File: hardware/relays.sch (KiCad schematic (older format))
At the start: 203 parts

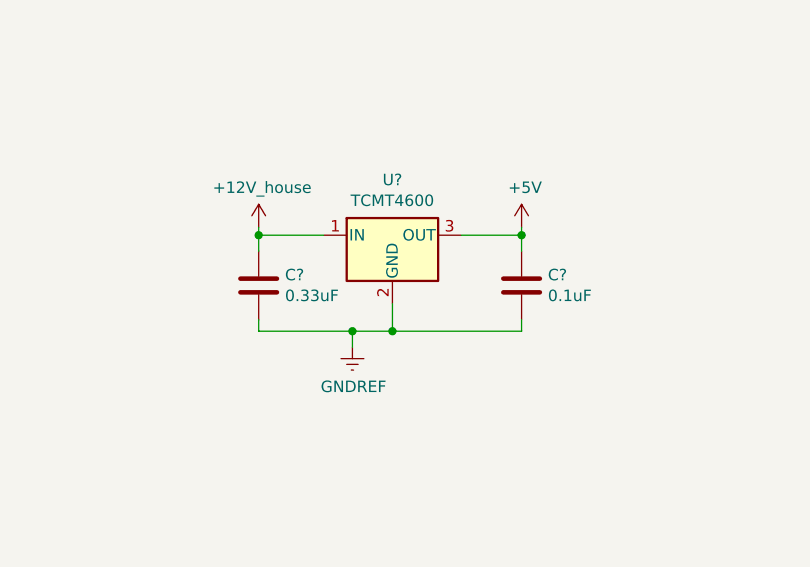
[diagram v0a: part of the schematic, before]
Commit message: hardware: add 5V domain for house and truck supplies
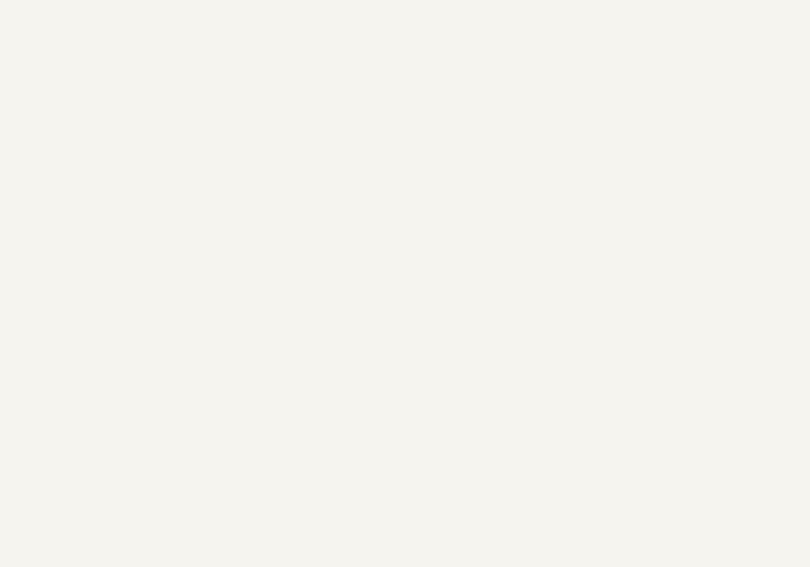
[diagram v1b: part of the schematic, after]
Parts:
- removed C?: 0.33uF, Capacitor_SMD:C_0805_2012Metric_Pad1.18x1.45mm_HandSolder, symbol Device:C
- removed C?: 0.1uF, Capacitor_SMD:C_0805_2012Metric_Pad1.18x1.45mm_HandSolder, symbol Device:C
- removed U?: TCMT4600, Package_SO:SOP-16_4.55x10.3mm_P1.27mm, symbol Regulator_Linear:L7805
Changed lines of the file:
@@
-$EndComp
-$Comp
-L Regulator_Linear:L7805 U?
-U 1 1 6096161B
-P 29230 5335
-F 0 "U?" H 29230 5577 50  0000 C CNN
-F 1 "TCMT4600" H 29230 5486 50  0000 C CNN
-F 2 "Package_SO:SOP-16_4.55x10.3mm_P1.27mm" H 29255 5185 50  0001 L CIN
-F 3 "http://www.vishay.com/docs/83512/tcmt1600.pdf" H 29230 5285 50  0001 C CNN
-	1    29230 5335
-	1    0    0    -1
-$EndComp
-$Comp
-L Device:C C?
-U 1 1 60963BB6
-P 28645 5555
-F 0 "C?" H 28760 5601 50  0000 L CNN
-F 1 "0.33uF" H 28760 5510 50  0000 L CNN
-F 2 "Capacitor_SMD:C_0805_2012Metric_Pad1.18x1.45mm_HandSolder" H 28683 5405 50  0001 C CNN
-F 3 "~" H 28645 5555 50  0001 C CNN
-	1    28645 5555
-	1    0    0    -1
-$EndComp
-$Comp
-L Device:C C?
-U 1 1 60964243
-P 29795 5555
-F 0 "C?" H 29910 5601 50  0000 L CNN
-F 1 "0.1uF" H 29910 5510 50  0000 L CNN
-F 2 "Capacitor_SMD:C_0805_2012Metric_Pad1.18x1.45mm_HandSolder" H 29833 5405 50  0001 C CNN
-F 3 "~" H 29795 5555 50  0001 C CNN
-	1    29795 5555
-	1    0    0    -1
-$EndComp
-Wire Wire Line
-	29530 5335 29795 5335
-Wire Wire Line
-	28645 5335 28930 5335
-Wire Wire Line
-	28645 5705 28645 5755
-Wire Wire Line
-	28645 5755 29055 5755
-Wire Wire Line
-	29795 5755 29795 5705
-Connection ~ 29230 5755
-Wire Wire Line
-	29230 5755 29795 5755
-$Comp
-L power:GNDREF #PWR?
-U 1 1 609665C9
-P 29055 5825
-F 0 "#PWR?" H 29055 5575 50  0001 C CNN
-F 1 "GNDREF" H 29060 5652 50  0000 C CNN
-F 2 "" H 29055 5825 50  0001 C CNN
-F 3 "" H 29055 5825 50  0001 C CNN
-	1    29055 5825
-	1    0    0    -1
-$EndComp
-Wire Wire Line
-	29055 5825 29055 5755
-Connection ~ 29055 5755
-Wire Wire Line
-	29055 5755 29230 5755
-Wire Wire Line
-	29230 5635 29230 5755
-Wire Wire Line
-	28645 5335 28645 5405
-Wire Wire Line
-	29795 5335 29795 5405
-Wire Wire Line
-	29795 5335 29795 5300
-Connection ~ 29795 5335
-Wire Wire Line
-	28645 5335 28645 5300
-Connection ~ 28645 5335
-$Comp
-L switchboard:+12V_house #PWR?
-U 1 1 6096CA71
-P 28645 5300
-F 0 "#PWR?" H 28645 5150 50  0001 C CNN
-F 1 "+12V_house" H 28660 5473 50  0000 C CNN
-F 2 "" H 28645 5300 50  0001 C CNN
-F 3 "" H 28645 5300 50  0001 C CNN
-	1    28645 5300
-	1    0    0    -1
-$EndComp
-$Comp
-L power:+5V #PWR?
-U 1 1 6096DC54
-P 29795 5300
-F 0 "#PWR?" H 29795 5150 50  0001 C CNN
-F 1 "+5V" H 29810 5473 50  0000 C CNN
-F 2 "" H 29795 5300 50  0001 C CNN
-F 3 "" H 29795 5300 50  0001 C CNN
-	1    29795 5300
-	1    0    0    -1
 $EndComp
 $Comp

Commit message: hardware: use 5V_house/truck nets for load drivers
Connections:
- net +5V: no longer U?.16

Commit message: hardware: fix weird bug with VN750 symbol
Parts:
- removed U? (x50): TCMT4600, Package_SO:SOP-16_4.55x10.3mm_P1.27mm, symbol switchboard:VN750
- added U? (x50): VN750, switchboard:VN750-B513TR, symbol switchboard:VN750
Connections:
- net AUX_1_OUT0: now also U?.3
- net AUX_1_OUT1: now also U?.5
- net AUX_2_OUT0: now also U?.3
- net AUX_2_OUT1: now also U?.5
- net AUX_3_OUT0: now also U?.3
- net AUX_3_OUT1: now also U?.5
- net AUX_4_OUT0: now also U?.3
- net AUX_4_OUT1: now also U?.5
- net BACKUP_ALARM0: now also U?.3
- net BACKUP_ALARM1: now also U?.5
- net BAR_LIGHT0: now also U?.3
- net BAR_LIGHT1: now also U?.5
- net BENCH_DOME_A0: now also U?.3
- net BENCH_DOME_A1: now also U?.5
- net BENCH_DOME_B0: now also U?.3
- net BENCH_DOME_B1: now also U?.5
- net COMP_1_LIGHT0: now also U?.3
- net COMP_1_LIGHT1: now also U?.5
- net COMP_2_LIGHT0: now also U?.3
- net COMP_2_LIGHT1: now also U?.5
- net COMP_3_LIGHT0: now also U?.3
- net COMP_3_LIGHT1: now also U?.5
- net COMP_4_LIGHT0: now also U?.3
- net COMP_4_LIGHT1: now also U?.5
- net COMP_5_LIGHT0: now also U?.3
- net COMP_5_LIGHT1: now also U?.5
- net COT_DOME_A0: now also U?.3
- net COT_DOME_A1: now also U?.5
- net COT_DOME_B0: now also U?.3
- net COT_DOME_B1: now also U?.5
- net CURB_FRONT_RED0: now also U?.3
- net CURB_FRONT_RED1: now also U?.5
- net CURB_REAR_RED0: now also U?.3
- net CURB_REAR_RED1: now also U?.5
- net DRIVER_FLOOD_A0: now also U?.3
- net DRIVER_FLOOD_A1: now also U?.5
- net DRIVER_FLOOD_B0: now also U?.3
- net DRIVER_FLOOD_B1: now also U?.5
- net FOG_CURB0: now also U?.3
- net FOG_CURB1: now also U?.5
- net FOG_STREET0: now also U?.3
- net FOG_STREET1: now also U?.5
- net GNDREF: now also U?.1 (GND), U?.1 (GND), U?.1 (GND), U?.1 (GND), U?.1 (GND), U?.1 (GND), U?.1 (GND), U?.1 (GND), U?.1 (GND), U?.1 (GND), U?.1 (GND), U?.1 (GND), U?.1 (GND), U?.1 (GND), U?.1 (GND), U?.1 (GND), U?.1 (GND), U?.1 (GND), U?.1 (GND), U?.1 (GND), U?.1 (GND), U?.1 (GND), U?.1 (GND), U?.1 (GND), U?.1 (GND), U?.1 (GND), U?.1 (GND), U?.1 (GND), U?.1 (GND), U?.1 (GND), U?.1 (GND), U?.1 (GND), U?.1 (GND), U?.1 (GND), U?.1 (GND), U?.1 (GND), U?.1 (GND), U?.1 (GND), U?.1 (GND), U?.1 (GND), U?.1 (GND), U?.1 (GND), U?.1 (GND), U?.1 (GND), U?.1 (GND), U?.1 (GND), U?.1 (GND), U?.1 (GND), U?.1 (GND), U?.1 (GND)
- net GRILLE_STROBE0: now also U?.3
- net GRILLE_STROBE1: now also U?.5
- net HEADLAMP_HI_L0: now also U?.3
- net HEADLAMP_HI_L1: now also U?.5
- net HEADLAMP_HI_R0: now also U?.3
- net HEADLAMP_HI_R1: now also U?.5
- net LIGHT_BAR_A0: now also U?.3
- net LIGHT_BAR_A1: now also U?.5
- net LIGHT_BAR_B0: now also U?.3
- net LIGHT_BAR_B1: now also U?.5
- net LIGHT_BAR_C0: now also U?.3
- net LIGHT_BAR_C1: now also U?.5
- net LIGHT_BAR_D0: now also U?.3
- net LIGHT_BAR_D1: now also U?.5
- net LIGHT_BAR_E0: now also U?.3
- net LIGHT_BAR_E1: now also U?.5
- net LIGHT_BAR_F0: now also U?.3
- net LIGHT_BAR_F1: now also U?.5
- net LIGHT_BAR_G0: now also U?.3
- net LIGHT_BAR_G1: now also U?.5
- net MARKER_LIGHTS_A0: now also U?.3
- net MARKER_LIGHTS_A1: now also U?.5
- net MARKER_LIGHTS_B0: now also U?.3
- net MARKER_LIGHTS_B1: now also U?.5
- net PACK_POWER_A0: now also U?.3
- net PACK_POWER_A1: now also U?.5
- net PACK_POWER_B0: now also U?.3
- net PACK_POWER_B1: now also U?.5
- net PASS_FLOOD_A0: now also U?.3
- net PASS_FLOOD_A1: now also U?.5
- net PASS_FLOOD_B0: now also U?.3
- net PASS_FLOOD_B1: now also U?.5
- net REAR_FLOOD_A0: now also U?.3
- net REAR_FLOOD_A1: now also U?.5
- net REAR_FLOOD_B0: now also U?.3
- net REAR_FLOOD_B1: now also U?.5
- net REAR_LOW_CURB0: now also U?.3
- net REAR_LOW_CURB1: now also U?.5
- net REAR_LOW_STREET0: now also U?.3
- net REAR_LOW_STREET1: now also U?.5
- net REAR_STROBE0: now also U?.3
- net REAR_STROBE1: now also U?.5
- net SECURITY_RELAY0: now also U?.3
- net SECURITY_RELAY1: now also U?.5
- net STREET_FRONT_RED0: now also U?.3
- net STREET_FRONT_RED1: now also U?.5
- net STREET_REAR_RED0: now also U?.3
- net STREET_REAR_RED1: now also U?.5
- net STRIP_LIGHT_C0: now also U?.3
- net STRIP_LIGHT_C1: now also U?.5
- net STRIP_LIGHT_F0: now also U?.3
- net STRIP_LIGHT_F1: now also U?.5
- net STRIP_LIGHT_R0: now also U?.3
- net STRIP_LIGHT_R1: now also U?.5
- net STROBE_PATTERN0: now also U?.3
- net STROBE_PATTERN1: now also U?.5
- net WATER_PUMP0: now also U?.3
- net WATER_PUMP1: now also U?.5
- net at R?.2, U?.15: now also U?.2 (x50)

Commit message: hardware: use VND5160J instead of VN750
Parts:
- removed R? (x50): 10k, Resistor_SMD:R_0805_2012Metric_Pad1.20x1.40mm_HandSolder, symbol Device:R_US
- removed R? (x45): 2k, Resistor_SMD:R_0805_2012Metric_Pad1.20x1.40mm_HandSolder, symbol Device:R_US
- removed U? (x50): TCMT4600, Package_SO:SOP-16_4.55x10.3mm_P1.27mm, symbol Isolator:TCMT4600
- removed U? (x49): VN750, switchboard:VN750-B513TR, symbol switchboard:VN750
- added R? (x33): 10k, Resistor_SMD:R_0805_2012Metric_Pad1.20x1.40mm_HandSolder, symbol Device:R_US
- added R? (x28): 2k, Resistor_SMD:R_0805_2012Metric_Pad1.20x1.40mm_HandSolder, symbol Device:R_US
- added U? (x42): VND5160J, switchboard:VND5160JTR-E, symbol switchboard:VND5160J
- added U? (x33): TCMT4600, Package_SO:SOP-16_4.55x10.3mm_P1.27mm, symbol Isolator:TCMT4600
- U?: value VN750 -> VND5160J; footprint switchboard:VN750-B513TR -> switchboard:VND5160JTR-E
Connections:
- net labels added: BACKUP_ALARM_CTRL_5V, BAR_LIGHT_CTRL_5V, COMP_1_LIGHT_CTRL_5V, COMP_2_LIGHT_CTRL_5V, COMP_3_LIGHT_CTRL_5V, COMP_4_LIGHT_CTRL_5V, COMP_5_LIGHT_CTRL_5V, CURB_FRONT_RED_CTRL_5V, CURB_REAR_RED_CTRL_5V, DOME_CTRL_5V, DRIVER_FLOOD_CTRL_5V, FOG_CTRL_5V, GRILLE_STROBE_CTRL_5V, LIGHT_BAR_A_CTRL_5V, LIGHT_BAR_B_CTRL_5V, LIGHT_BAR_C_CTRL_5V, LIGHT_BAR_D_CTRL_5V, LIGHT_BAR_E_CTRL_5V, LIGHT_BAR_F_CTRL_5V, LIGHT_BAR_G_CTRL_5V, MARKER_CTRL_5V, PACK_POWER_CTRL_5V, PASS_FLOOD_CTRL_5V, REAR_FLOOD_CTRL_5V, REAR_LOW_CURB_CTRL_5V, REAR_LOW_STREET_CTRL_5V, REAR_STROBE_CTRL_5V, SECURITY_RELAY_CTRL_5V, STREET_FRONT_RED_CTRL_5V, STREET_REAR_RED_CTRL_5V, STRIP_LIGHT_CTRL_5V, STROBE_PATTERN_CTRL_5V
- net labels removed: AUX_1_CTRL_12V, AUX_1_OUT0, AUX_1_OUT1, AUX_1_OUT[0..1], AUX_2_CTRL_12V, AUX_2_OUT0, AUX_2_OUT1, AUX_2_OUT[0..1], AUX_3_CTRL_12V, AUX_3_OUT0, AUX_3_OUT1, AUX_3_OUT[0..1], AUX_4_CTRL_12V, AUX_4_OUT0, AUX_4_OUT1, AUX_4_OUT[0..1], COT_DOME_B0, HEADLAMP_HI_L0, HEADLAMP_HI_L1, HEADLAMP_HI_L[0..1], HEADLAMP_HI_L_CTRL_12V, HEADLAMP_HI_R0, HEADLAMP_HI_R1, HEADLAMP_HI_R[0..1], HEADLAMP_HI_R_CTRL_12V, WATER_PUMP0, WATER_PUMP1, WATER_PUMP[0..1], WATER_PUMP_CTRL_12V
- wire segments 800 -> 570
- no-connect marks 50 -> 65
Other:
- note added: "Must standalone"
- note added: "TODO: Add Chassis Horn"
- note added: "Unit B is COMP_1_LIGHT"
- note removed: "Interior Components"
- moved on the sheet: R?, U?
